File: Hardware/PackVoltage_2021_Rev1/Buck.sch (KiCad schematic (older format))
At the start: 8 parts, among them J2 Test_Point

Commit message: added hierarchical labels, changed current sensor, added 12V labels to TIVA, finished buck sheet
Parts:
- added C3, C5: 100uF, symbol Device:C
- added C4, C6: 1000uF, symbol Device:C
- added D3, D5: D_Schottky, symbol Device:D_Schottky
- added D4, D6: LED, symbol Device:LED
- added J3V3, J5V: Test_Point, symbol MRDT_Connectors:Test_Point
- added L? (x2): 100uH, symbol Device:L
- added R2: 510, symbol Device:R
- added R3: 330, symbol Device:R
- added U? (x2): LM2576D2TR4, symbol MRDT_Devices:LM2576D2TR4
- renumbered D3 to D1, D4 to D2, J2 to J12V, R2 to R1
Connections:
- net +12V: now also C3.2, C5.2, U?.1 (VIN), U?.1 (VIN)
- net GND: now also C3.1, C4.2, C5.1, C6.2, D3.2 (A), D5.2 (A), R2.1, R3.1, U?.3 (GND), U?.3 (GND), U?.5 (ON/OFF), U?.5 (ON/OFF), U?.6 (TAB), U?.6 (TAB)
- net 33.6V renamed PV
- new net: D3.1 (K), L?.2, U?.2 (OUTPUT)
- new net: D4.1 (K), R2.2
- new net: D5.1 (K), L?.2, U?.2 (OUTPUT)
- new net: D6.1 (K), R3.2
- new net +3V3: C6.1, D6.2 (A), J3V3.1, L?.1, U?.4 (FEEDBACK)
- new net +5V: C4.1, D4.2 (A), J5V.1, L?.1, U?.4 (FEEDBACK)

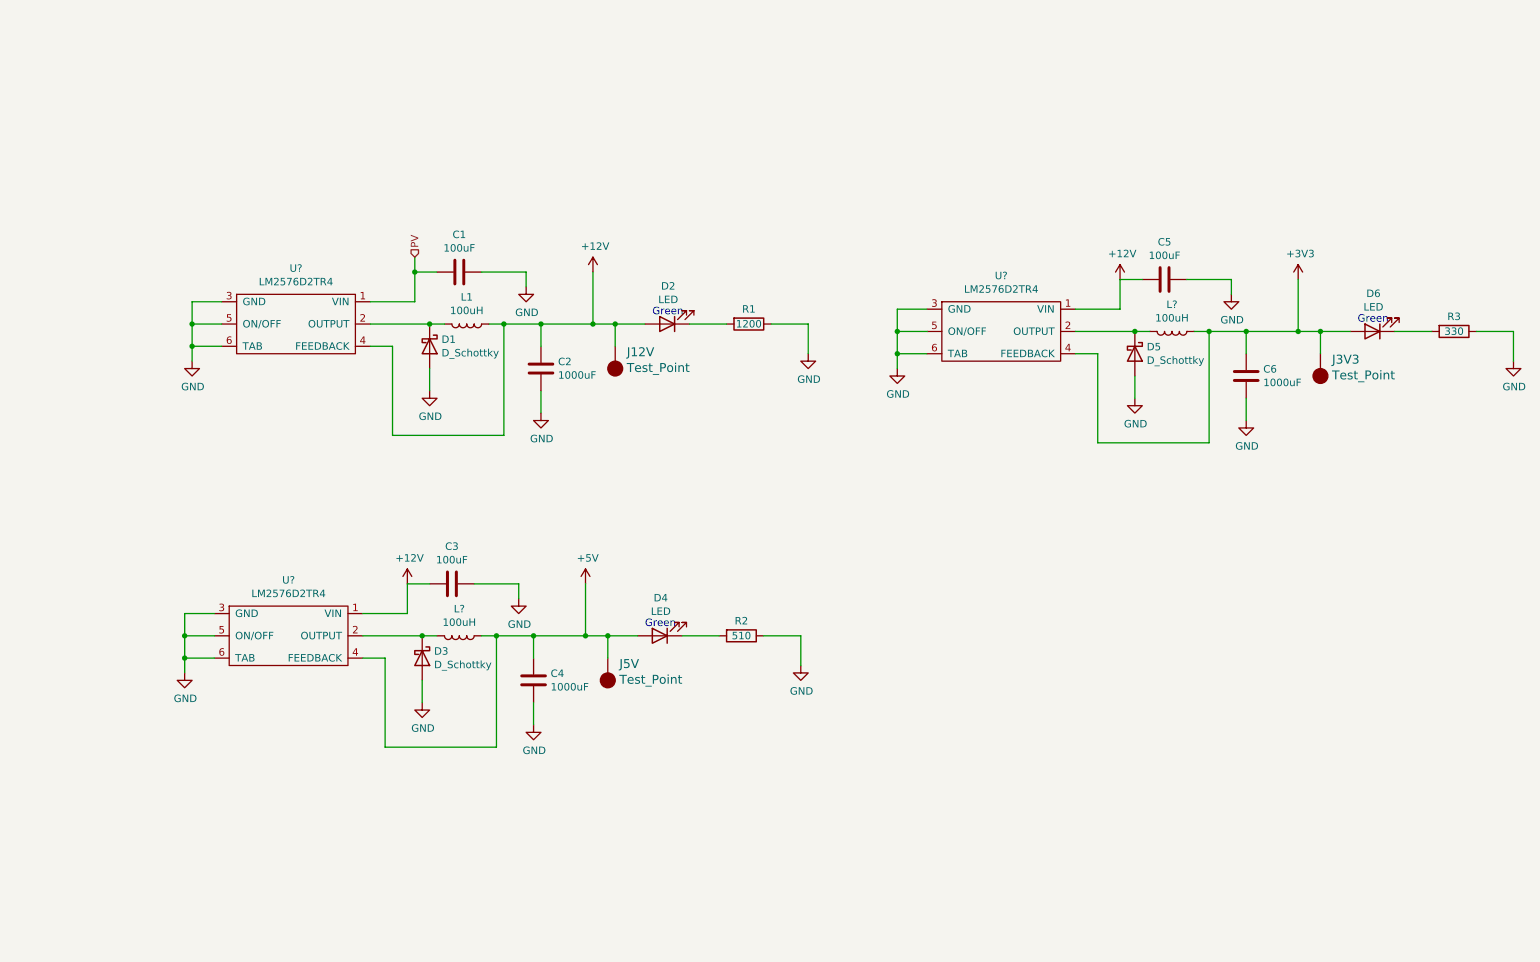
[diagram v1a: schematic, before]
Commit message: Annotated Sheet, added Busses, Moved Andersons
Autocompleted annotations for sheet
Duplicated bus for Motor 1 to all other busses, split "Busses" sheet into "Motor Busses" and "Other Busses" for space.
Moved andersons from bus sheets to top level sheet.
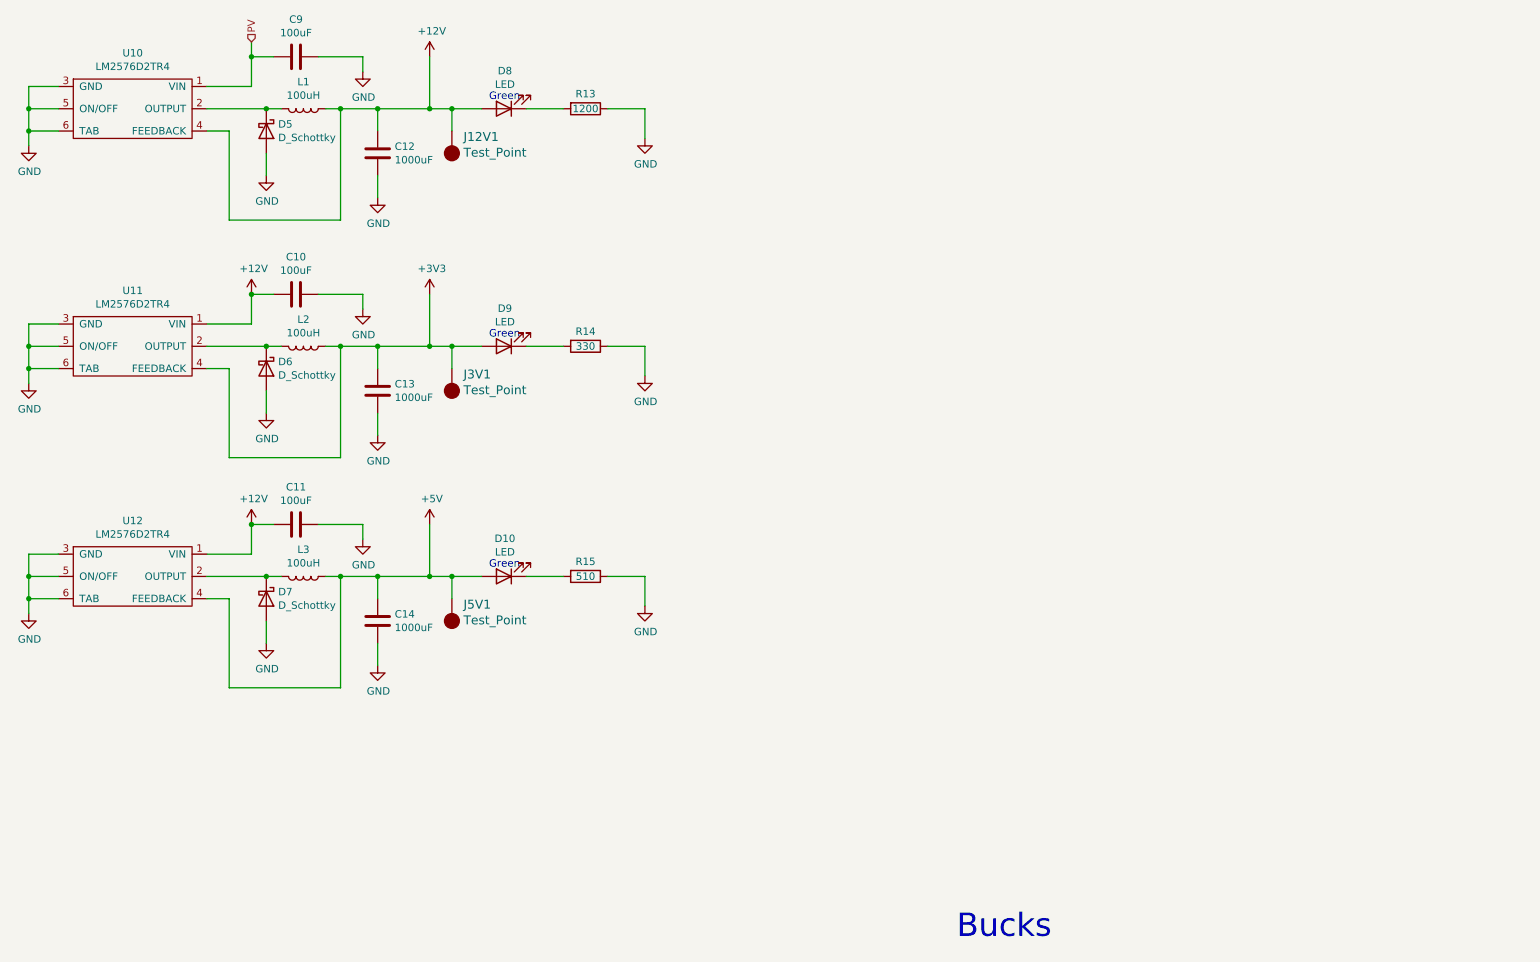
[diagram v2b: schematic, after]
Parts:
- gave numbers to parts that had none: 5
- renumbered C5 to C10, C3 to C11, C2 to C12, C6 to C13, C4 to C14, C1 to C9, D4 to D10, D1 to D5, D5 to D6, D3 to D7, D2 to D8, D6 to D9, J12V to J12V1, J3V3 to J3V1, J5V to J5V1, R1 to R13, R3 to R14, R2 to R15
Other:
- note added: "Bucks"
- moved on the sheet: C10, C11, C12, C13, C14, C9, D10, D5, D6, D7, D8, D9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

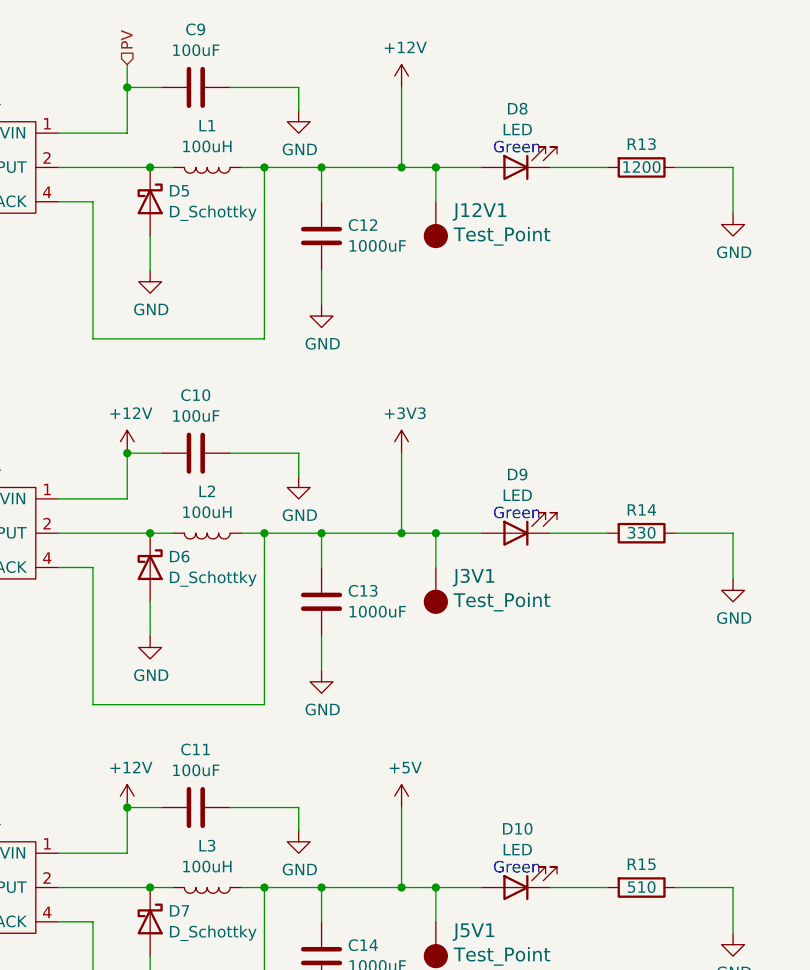
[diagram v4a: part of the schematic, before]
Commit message: Fixed Hierarchial Pins/Labels
Removed Hierarchal labels from top sheet and replaced them with pins linked to the subsheets.
Renamed M5 Tiva pin to D1
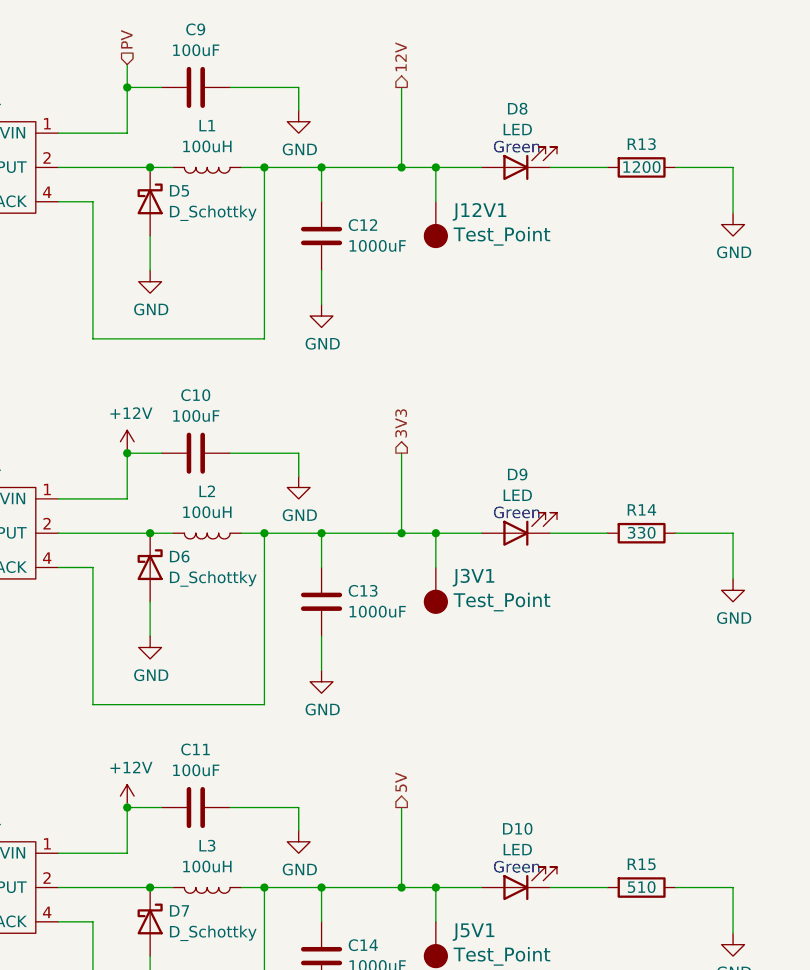
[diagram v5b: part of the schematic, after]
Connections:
- net +12V: no longer C12.1, D8.2 (A), J12V1.1, L1.1, U10.4 (FEEDBACK)
- net +3V3 renamed 3V3
- net +5V renamed 5V
- new net 12V: C12.1, D8.2 (A), J12V1.1, L1.1, U10.4 (FEEDBACK)
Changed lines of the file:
@@
 Wire Wire Line
 	3250 1800 3250 1950
-$Comp
-L power:+12V #PWR042
-U 1 1 5F82E98F
-P 3600 1000
-F 0 "#PWR042" H 3600 850 50  0001 C CNN
-F 1 "+12V" H 3615 1173 50  0000 C CNN
-F 2 "" H 3600 1000 50  0001 C CNN
-F 3 "" H 3600 1000 50  0001 C CNN
-	1    3600 1000
-	1    0    0    -1
-$EndComp
 Wire Wire Line
 	3250 1350 3600 1350
@@
 $EndComp
 $Comp
-L power:+5V #PWR044
-U 1 1 5F87265E
-P 3600 4150
-F 0 "#PWR044" H 3600 4000 50  0001 C CNN
-F 1 "+5V" H 3615 4323 50  0000 C CNN
-F 2 "" H 3600 4150 50  0001 C CNN
-F 3 "" H 3600 4150 50  0001 C CNN
-	1    3600 4150
-	1    0    0    -1
-$EndComp
-$Comp
 L MRDT_Devices:LM2576D2TR4 U11
 U 1 1 5F874FF1
@@
 	1    0    0    -1
 $EndComp
-$Comp
-L power:+3V3 #PWR043
-U 1 1 5F8789F3
-P 3600 2600
-F 0 "#PWR043" H 3600 2450 50  0001 C CNN
-F 1 "+3V3" H 3615 2773 50  0000 C CNN
-F 2 "" H 3600 2600 50  0001 C CNN
-F 3 "" H 3600 2600 50  0001 C CNN
-	1    3600 2600
-	1    0    0    -1
-$EndComp
 Text HLabel 2400 900  1    50   Input ~ 0
 PV
@@
 Text Notes 7150 6950 0    157  ~ 0
 Bucks
+Text HLabel 3600 1000 1    50   Output ~ 0
+12V
+Text HLabel 3600 4150 1    50   Output ~ 0
+5V
+Text HLabel 3600 2600 1    50   Output ~ 0
+3V3
 $EndSCHEMATC

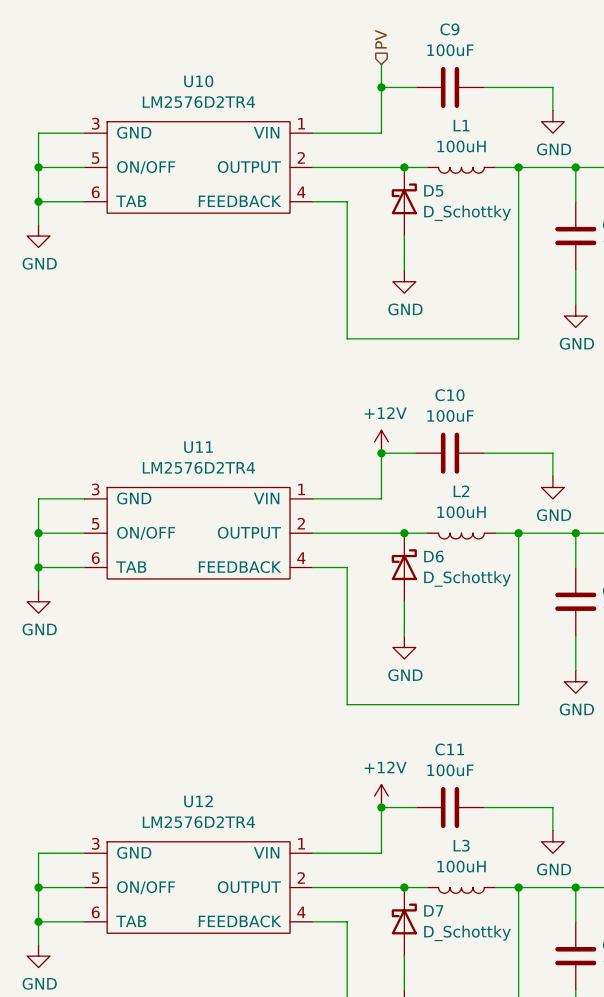
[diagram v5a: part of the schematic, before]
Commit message: corrected orientation of ground symbols, renamed buck converters, still need to update tiva with extra 12V pin
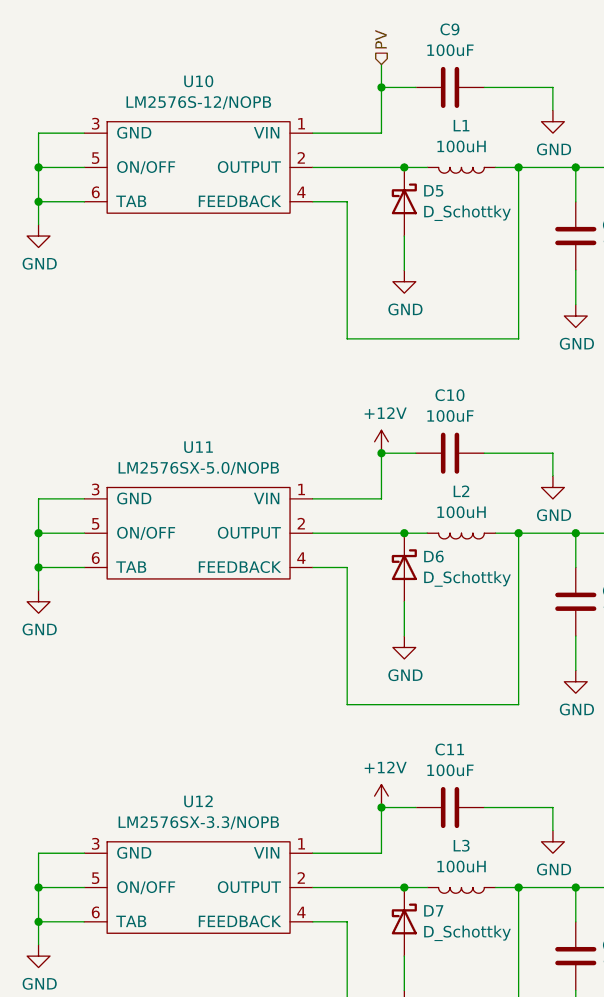
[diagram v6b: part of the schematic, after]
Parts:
- U10: value LM2576D2TR4 -> LM2576S-12/NOPB
- U11: value LM2576D2TR4 -> LM2576SX-5.0/NOPB
- U12: value LM2576D2TR4 -> LM2576SX-3.3/NOPB
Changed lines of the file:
@@
 $EndDescr
-$Comp
-L MRDT_Devices:LM2576D2TR4 U10
-U 1 1 5F826D23
-P 1600 1400
-F 0 "U10" H 1600 1825 50  0000 C CNN
-F 1 "LM2576D2TR4" H 1600 1734 50  0000 C CNN
-F 2 "" H 1600 1850 50  0001 C CNN
-F 3 "https://www.mouser.com/datasheet/2/308/LM2576_D-1810688.pdf" H 1600 1850 50  0001 C CNN
-	1    1600 1400
-	1    0    0    -1
-$EndComp
 $Comp
 L power:GND #PWR028
@@
 P 1600 4550
 F 0 "U12" H 1600 4975 50  0000 C CNN
-F 1 "LM2576D2TR4" H 1600 4884 50  0000 C CNN
+F 1 "LM2576SX-3.3/NOPB" H 1600 4884 50  0000 C CNN
 F 2 "" H 1600 5000 50  0001 C CNN
 F 3 "https://www.mouser.com/datasheet/2/308/LM2576_D-1810688.pdf" H 1600 5000 50  0001 C CNN
@@
 P 1600 3000
 F 0 "U11" H 1600 3425 50  0000 C CNN
-F 1 "LM2576D2TR4" H 1600 3334 50  0000 C CNN
+F 1 "LM2576SX-5.0/NOPB" H 1600 3334 50  0000 C CNN
 F 2 "" H 1600 3450 50  0001 C CNN
 F 3 "https://www.mouser.com/datasheet/2/308/LM2576_D-1810688.pdf" H 1600 3450 50  0001 C CNN
@@
 Text HLabel 3600 2600 1    50   Output ~ 0
 3V3
+$Comp
+L MRDT_Devices:LM2576D2TR4 U10
+U 1 1 5F826D23
+P 1600 1400
+F 0 "U10" H 1600 1825 50  0000 C CNN
+F 1 "LM2576S-12/NOPB" H 1600 1734 50  0000 C CNN
+F 2 "" H 1600 1850 50  0001 C CNN
+F 3 "https://www.mouser.com/datasheet/2/308/LM2576_D-1810688.pdf" H 1600 1850 50  0001 C CNN
+	1    1600 1400
+	1    0    0    -1
+$EndComp
 $EndSCHEMATC
